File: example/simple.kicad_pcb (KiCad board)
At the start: 2 copper layers, 7.6 x 10.2 mm, 5 parts, among them J1 Conn_01x03, J2 Conn_01x03, J3 Conn_02x03_Counter_Clockwise, J4 Conn_02x03_Counter_Clockwise

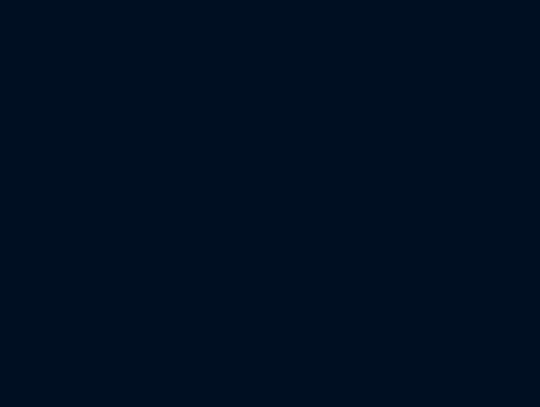
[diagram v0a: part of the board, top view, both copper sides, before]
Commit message: Bezier curves in PCBs done, zones in progress
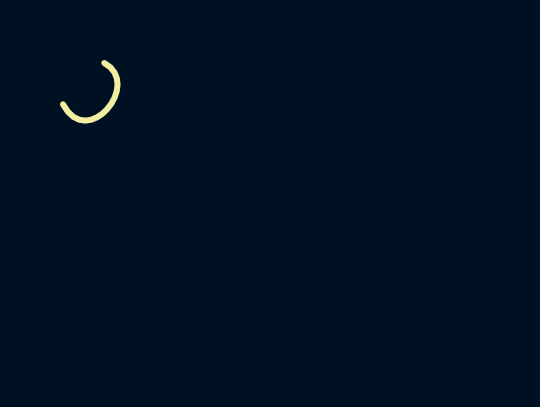
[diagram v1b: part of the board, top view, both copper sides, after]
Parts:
- moved G*** 9.85 mm to (53.5, 34.3)
